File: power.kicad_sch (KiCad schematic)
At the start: 84 parts, among them U3 TLV62569DBV, U4 TLV62569DBV, U5 TLV62569DBV, Y2 32768Hz

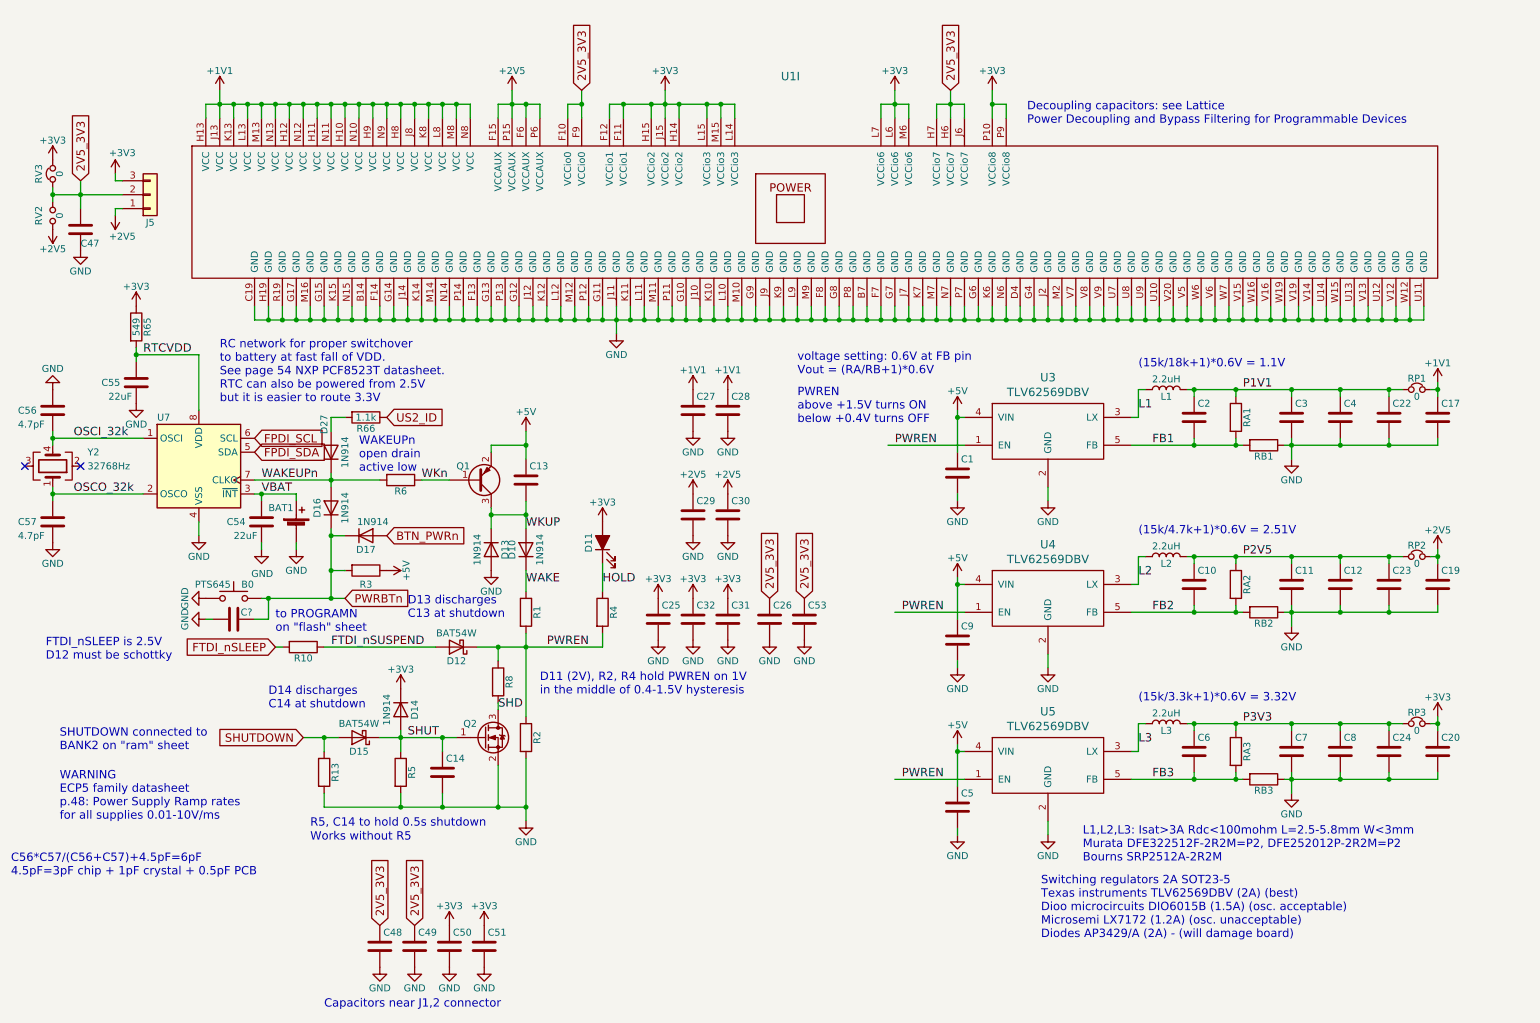
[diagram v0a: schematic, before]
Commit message: Adding USB-C
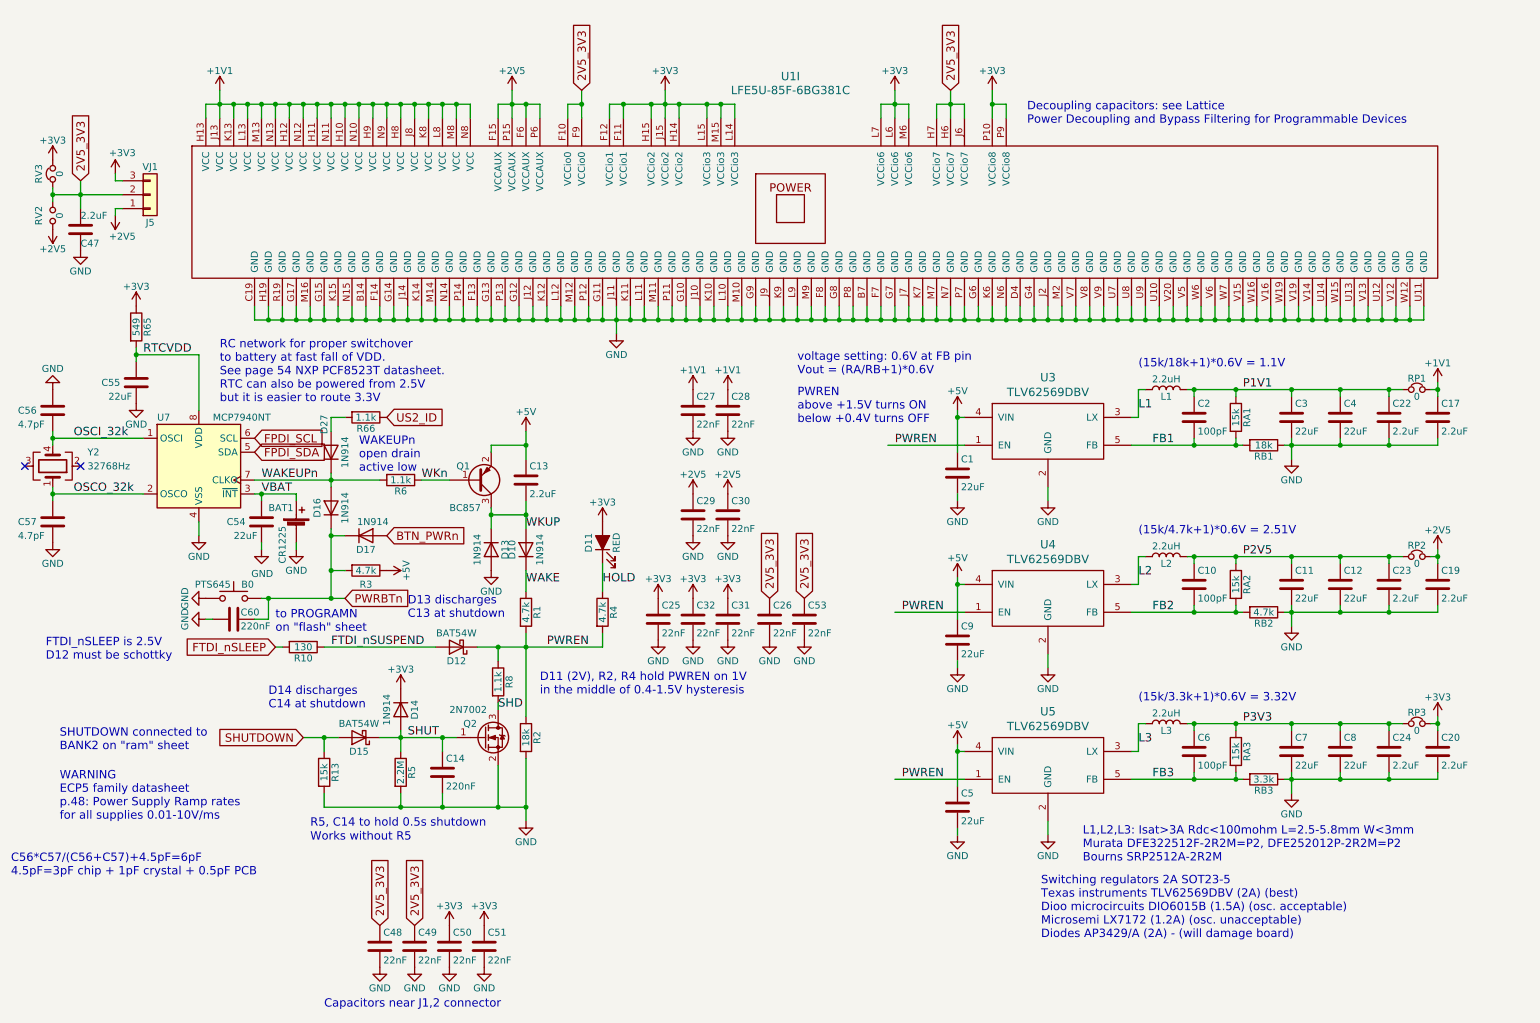
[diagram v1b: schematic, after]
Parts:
- BAT1: value (none) -> CR1225; footprint (none) -> Keystone_3000_1x12mm-CoinCell:Keystone_3000_1x12mm-CoinCell
- C1, C11, C12, C3, C4, C5, C7, C8, C9: value (none) -> 22uF; footprint (none) -> Capacitor_SMD:C_0805_2012Metric
- C10, C2, C6: value (none) -> 100pF; footprint (none) -> Capacitor_SMD:C_0603_1608Metric
- C13, C17, C19, C20, C22, C23, C24, C47: value (none) -> 2.2uF; footprint (none) -> Capacitor_SMD:C_0805_2012Metric
- C14: value (none) -> 220nF; footprint (none) -> Capacitor_SMD:C_0603_1608Metric
- C25, C26, C27, C28, C29, C30, C31, C32, C48, C49, C50, C51, C53: value (none) -> 22nF; footprint (none) -> Capacitor_SMD:C_0603_1608Metric
- C60: renamed from C?; value (none) -> 220nF; footprint (none) -> Capacitor_SMD:C_0603_1608Metric
- D11: value (none) -> RED; footprint (none) -> LED_SMD:LED_0805_2012Metric
- J5: value (none) -> VJ1; footprint (none) -> Connector_PinHeader_2.54mm:PinHeader_1x03_P2.54mm_Vertical
- Q1: value (none) -> BC857; footprint (none) -> Package_TO_SOT_SMD:SOT-23
- Q2: value (none) -> 2N7002; footprint (none) -> Package_TO_SOT_SMD:SOT-23
- R1, R3, R4, RB2: value (none) -> 4.7k; footprint (none) -> Resistor_SMD:R_0603_1608Metric
- R10: value (none) -> 130; footprint (none) -> Resistor_SMD:R_0603_1608Metric
- R13, RA1, RA2, RA3: value (none) -> 15k; footprint (none) -> Resistor_SMD:R_0603_1608Metric
- R2, RB1: value (none) -> 18k; footprint (none) -> Resistor_SMD:R_0603_1608Metric
- R5: value (none) -> 2.2M; footprint (none) -> Resistor_SMD:R_0603_1608Metric
- R6, R8: value (none) -> 1.1k; footprint (none) -> Resistor_SMD:R_0603_1608Metric
- RB3: value (none) -> 3.3k; footprint (none) -> Resistor_SMD:R_0603_1608Metric
- U1: value (none) -> LFE5U-85F-6BG381C; footprint (none) -> lfe5bg381:BGA-381_pitch0.8mm_dia0.4mm
- U7: value (none) -> MCP7940NT; footprint (none) -> SOT96-1:SOT96-1

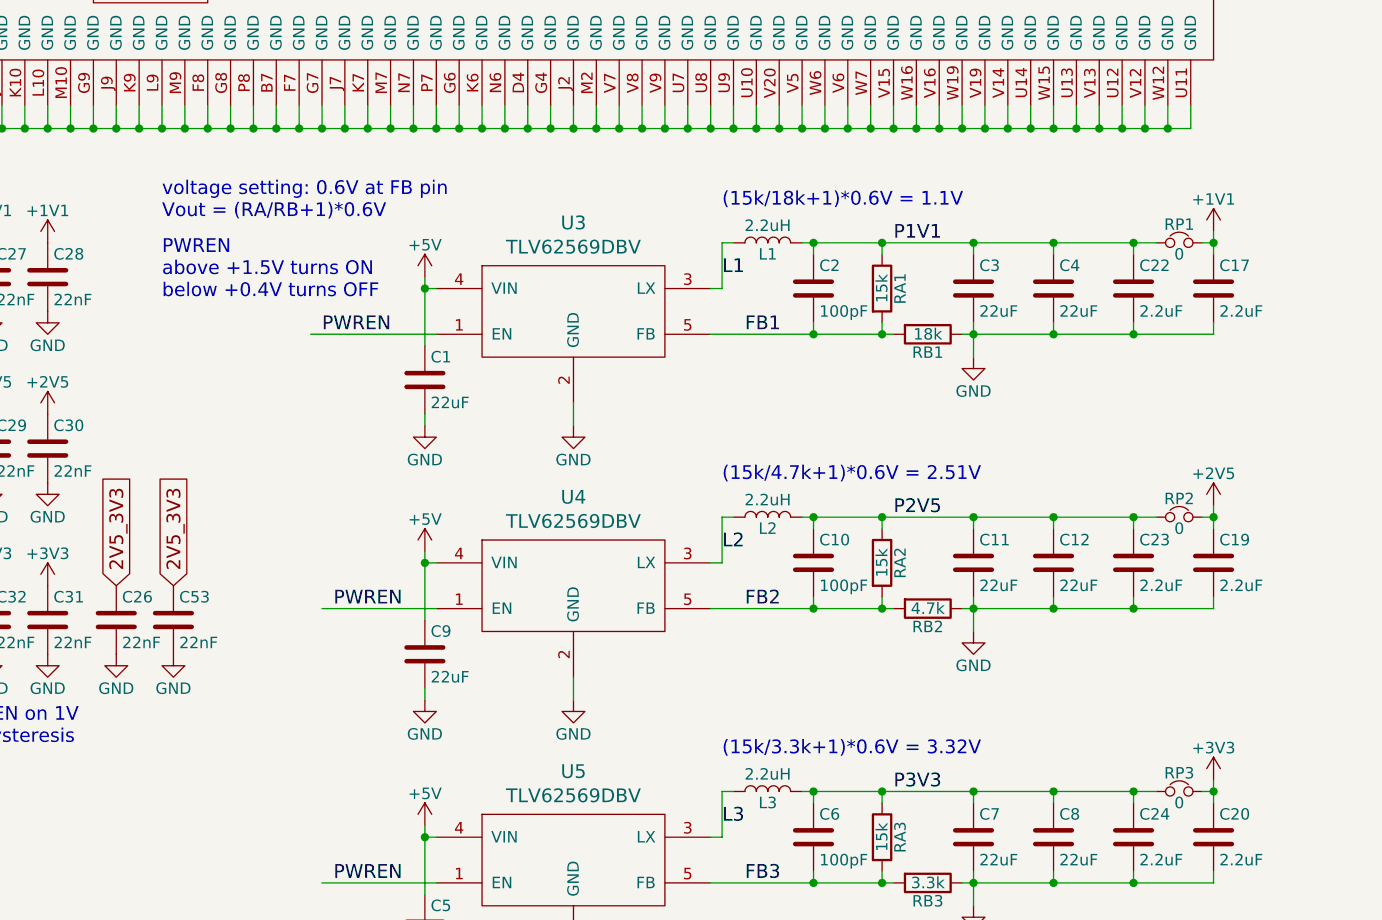
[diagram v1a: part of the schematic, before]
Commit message: Adding 1.2V option - fixing 3D view
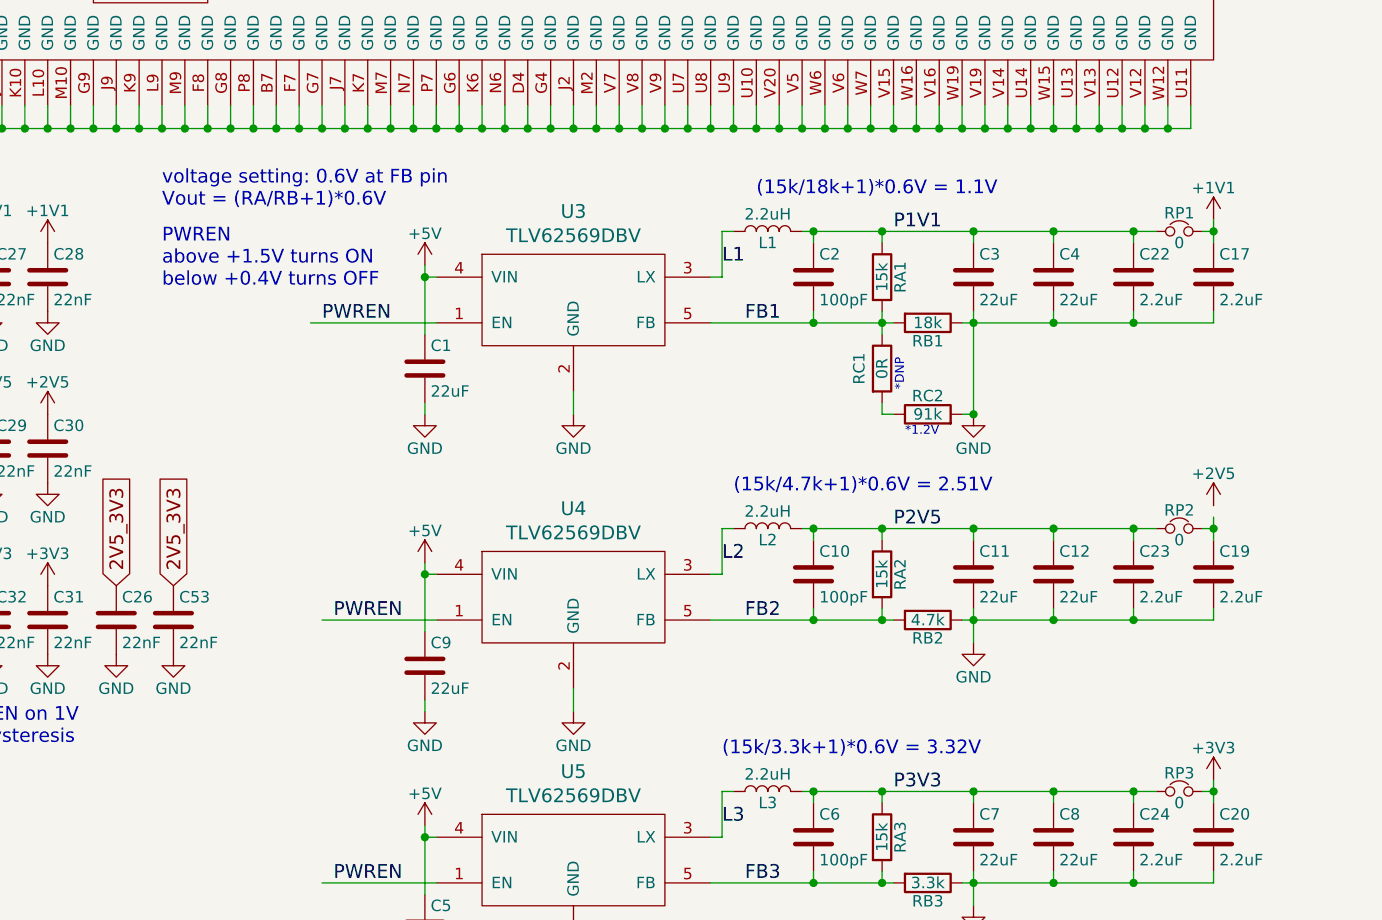
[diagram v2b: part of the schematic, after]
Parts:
- added RC1: 0R, Resistor_SMD:R_0603_1608Metric, symbol Device:R
- added RC2: 91k, Resistor_SMD:R_0603_1608Metric, symbol Device:R
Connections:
- net +2V5: no longer C19.1, RP2.2
- net FB1: now also RC1.1
- net GND: now also RC2.2
- new net: C19.1, RP2.2
- new net: RC1.2, RC2.1
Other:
- note added: "*1.2V"
- note added: "*DNP"
- moved on the sheet: C1, C10, C11, C12, C17, C19, C2, C22, C23, C3, C4, C9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
